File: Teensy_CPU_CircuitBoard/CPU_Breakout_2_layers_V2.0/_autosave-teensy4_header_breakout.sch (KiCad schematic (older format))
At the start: 17 parts, among them U1 MCP2542WFDxMF, U2 NUCLEO-H745ZI-Q, U3 MCP2542WFDxMF

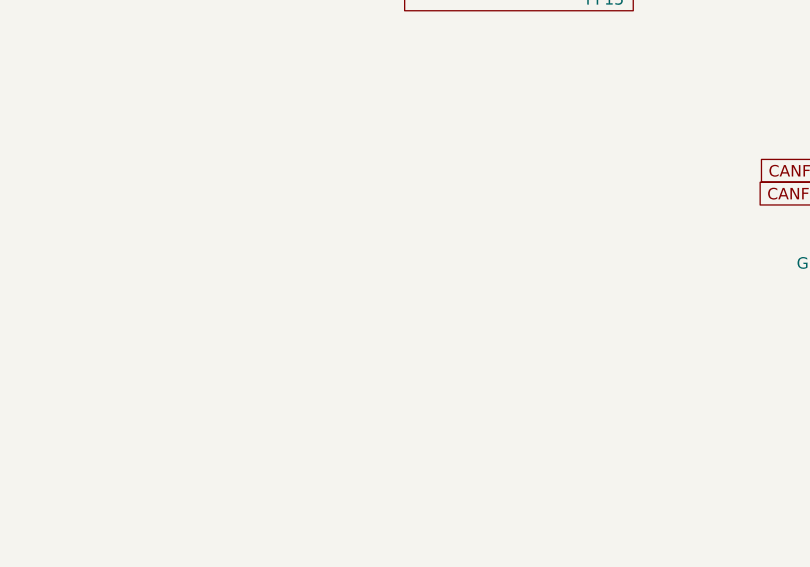
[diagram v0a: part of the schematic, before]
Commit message: PCB trace 1.0V
Har ikke lagt til spenningsforsyning til sensorene eller GND. Dessuten har jeg satt connectoren feil vei
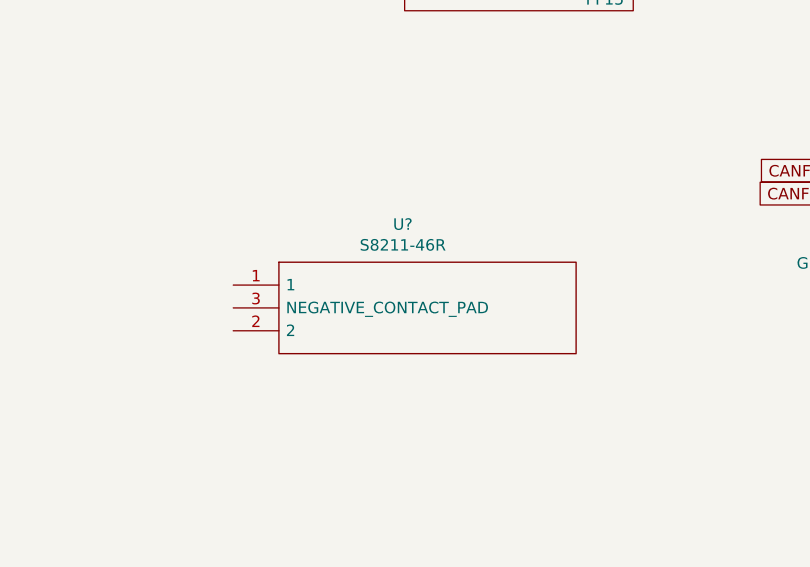
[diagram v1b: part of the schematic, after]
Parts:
- added U?: S8211-46R, S8211-46R, symbol teensy4_header_breakout-cache:S8211-46R
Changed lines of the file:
@@
 Wire Wire Line
 	2650 2150 2650 2250
+$Comp
+L teensy4_header_breakout-cache:S8211-46R U?
+U 1 1 60084389
+P 4650 5900
+F 0 "U?" H 5392 6165 50  0000 C CNN
+F 1 "S8211-46R" H 5392 6074 50  0000 C CNN
+F 2 "S8211-46R" H 6200 6000 50  0001 L CNN
+F 3 "https://cdn.harwin.com/pdfs/S8211R.pdf" H 6200 5900 50  0001 L CNN
+F 4 "HARWIN - S8211-46R - HOLDER, EZ-COIN, CR/BR2032 CELLS" H 6200 5800 50  0001 L CNN "Description"
+F 5 "HARWIN" H 6200 5600 50  0001 L CNN "Manufacturer_Name"
+F 6 "S8211-46R" H 6200 5500 50  0001 L CNN "Manufacturer_Part_Number"
+F 7 "855-S8211-46R" H 6200 5400 50  0001 L CNN "Mouser Part Number"
+F 8 "https://www.mouser.com/Search/Refine.aspx?Keyword=855-S8211-46R" H 6200 5300 50  0001 L CNN "Mouser Price/Stock"
+	1    4650 5900
+	1    0    0    -1
+$EndComp
 $EndSCHEMATC
